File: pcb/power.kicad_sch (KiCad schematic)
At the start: 5 parts, among them U3 AP2112K-3.3TRG1

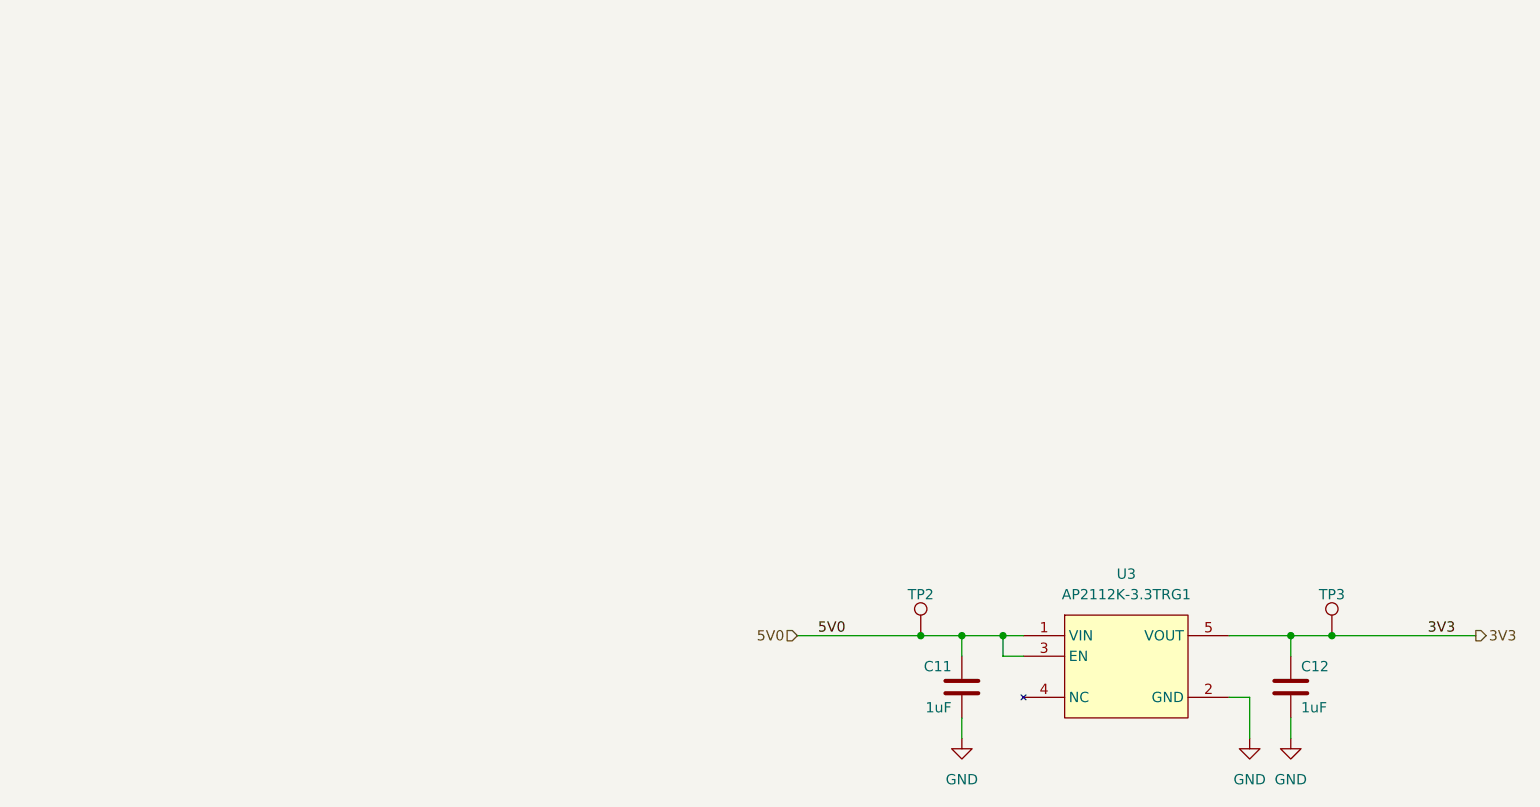
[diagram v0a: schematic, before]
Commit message: reroute matrix
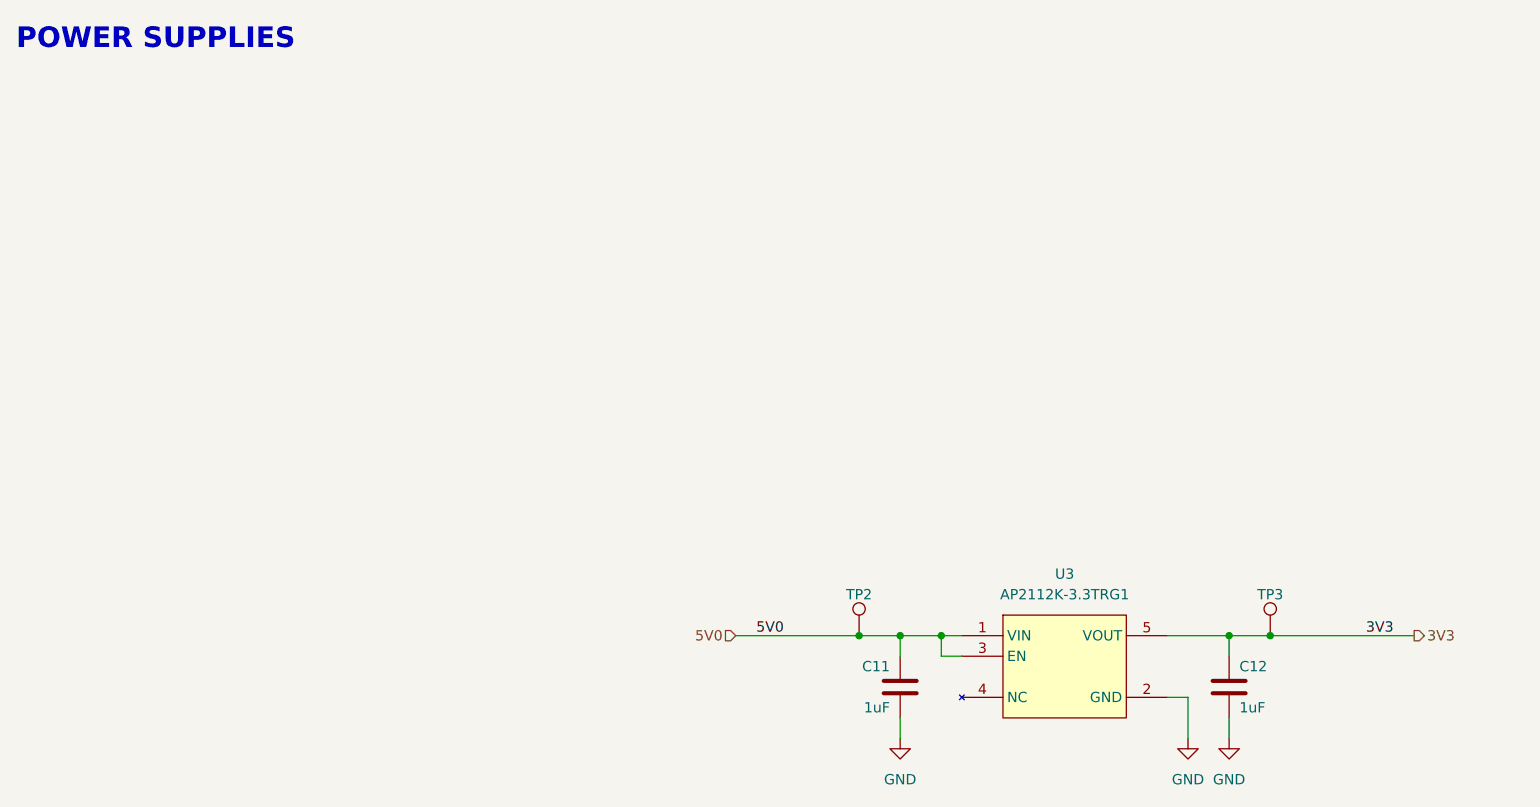
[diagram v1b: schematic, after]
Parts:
- C11, C12: footprint Capacitor_SMD:C_0402_1005Metric -> Capacitor_SMD:C_0603_1608Metric; Manufacturer Product Number C0402C105K9PACTU -> C0603C105K4RACTU
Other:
- note added: "POWER SUPPLIES"
- company: (none) -> ASE, ASW, AMB
- title: (none) -> ALANA-KB PCB
- moved on the sheet: C11, C12, TP2, TP3, U3
